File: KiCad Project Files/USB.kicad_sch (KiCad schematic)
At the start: 0 parts

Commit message: Complete schematic aside from switch matrix, and rename project
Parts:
- added C_LD01, C_LD02: 1u, symbol Device:C_Small
- added F1: 500mA, symbol Device:Polyfuse_Small
- added J1: SM04B, symbol Connector:Conn_01x04_Female
- added U4: PRTR5V0U2X, symbol cipulot_parts:PRTR5V0U2X
- added U?: XC6206PxxxMR, Package_TO_SOT_SMD:SOT-23, symbol Regulator_Linear:XC6206PxxxMR
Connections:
- new net +3V3: C_LD02.1, U?.2 (VO)
- new net +5V: C_LD01.1, F1.2, J1.1 (Pin_1), U?.3 (VI)
- new net D+: J1.3 (Pin_3), U4.2 (IO1)
- new net D-: J1.2 (Pin_2), U4.3 (IO2)
- new net GND: C_LD01.2, C_LD02.2, J1.4 (Pin_4), U4.1 (GND), U?.1 (GND)
- new net VCC: F1.1, U4.4 (VCC)
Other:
- note added: "ESD, Power Regulation & Protection"
- note added: "JST"

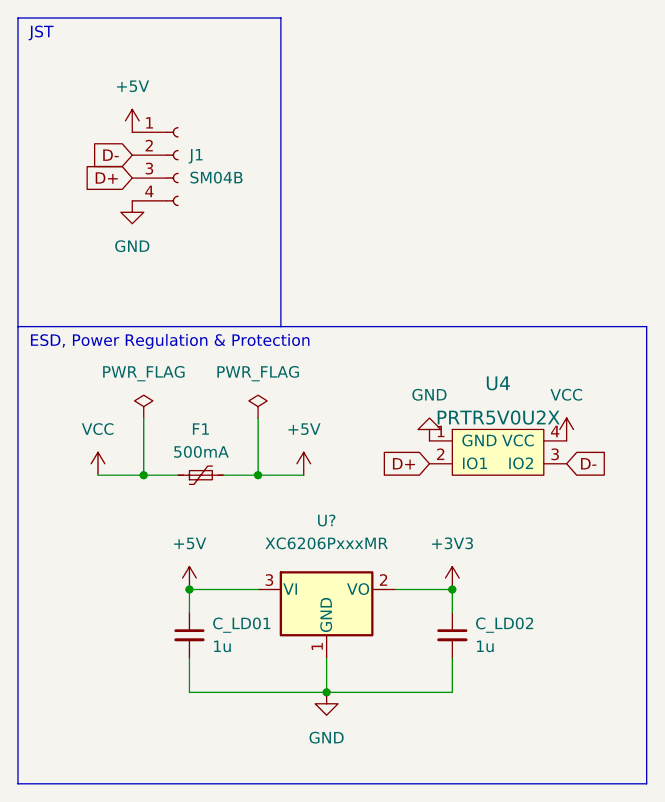
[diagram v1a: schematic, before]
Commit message: Finish schematic, annotate footprints, start pcb creation
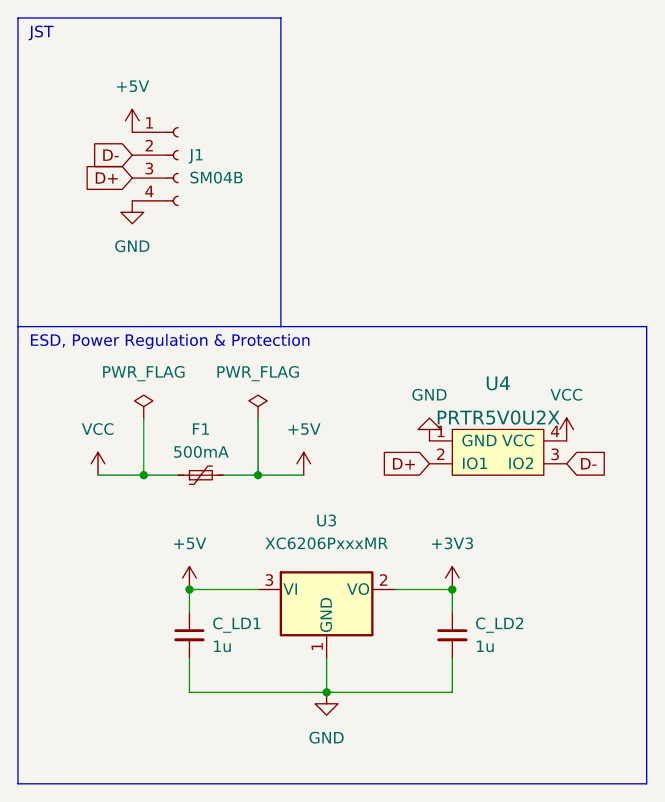
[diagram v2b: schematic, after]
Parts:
- C_LD1: renamed from C_LD01; footprint (none) -> Capacitor_SMD:C_0402_1005Metric
- C_LD2: renamed from C_LD02; footprint (none) -> Capacitor_SMD:C_0402_1005Metric
- F1: footprint (none) -> Fuse:Fuse_0805_2012Metric
- J1: footprint (none) -> Connector_JST:JST_SH_SM04B-SRSS-TB_1x04-1MP_P1.00mm_Horizontal
- U4: footprint (none) -> random-keyboard-parts:SOT143B
- gave numbers to parts that had none: 1
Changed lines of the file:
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@@
   (symbol (lib_id "power:+5V") (at 31.75 76.2 0) (unit 1)
     (in_bom yes) (on_board yes) (fields_autoplaced)
-    (property "Reference" "#PWR?" (id 0) (at 31.75 80.01 0)
+    (property "Reference" "#PWR0123" (id 0) (at 31.75 80.01 0)
       (effects (font (size 1.27 1.27)) hide)
     )
@@
       (effects (font (size 1.27 1.27)) (justify left))
     )
-    (property "Footprint" "" (id 2) (at 30.48 27.94 0)
+    (property "Footprint" "Connector_JST:JST_SH_SM04B-SRSS-TB_1x04-1MP_P1.00mm_Horizontal" (id 2) (at 30.48 27.94 0)
       (effects (font (size 1.27 1.27)) hide)
     )
@@
   (symbol (lib_id "Device:C_Small") (at 31.75 81.28 0) (unit 1)
     (in_bom yes) (on_board yes) (fields_autoplaced)
-    (property "Reference" "C_LD01" (id 0) (at 34.29 80.0162 0)
+    (property "Reference" "C_LD1" (id 0) (at 34.29 80.0162 0)
       (effects (font (size 1.27 1.27)) (justify left))
     )
@@
       (effects (font (size 1.27 1.27)) (justify left))
     )
-    (property "Footprint" "" (id 2) (at 31.75 81.28 0)
+    (property "Footprint" "Capacitor_SMD:C_0402_1005Metric" (id 2) (at 31.75 81.28 0)
       (effects (font (size 1.27 1.27)) hide)
     )
@@
   (symbol (lib_id "power:PWR_FLAG") (at 26.67 57.15 0) (unit 1)
     (in_bom yes) (on_board yes) (fields_autoplaced)
-    (property "Reference" "#FLG?" (id 0) (at 26.67 55.245 0)
+    (property "Reference" "#FLG0101" (id 0) (at 26.67 55.245 0)
       (effects (font (size 1.27 1.27)) hide)
     )
@@
   (symbol (lib_id "power:VCC") (at 73.66 59.69 0) (unit 1)
     (in_bom yes) (on_board yes) (fields_autoplaced)
-    (property "Reference" "#PWR?" (id 0) (at 73.66 63.5 0)
+    (property "Reference" "#PWR0119" (id 0) (at 73.66 63.5 0)
       (effects (font (size 1.27 1.27)) hide)
     )
@@
   (symbol (lib_id "power:GND") (at 58.42 59.69 180) (unit 1)
     (in_bom yes) (on_board yes) (fields_autoplaced)
-    (property "Reference" "#PWR?" (id 0) (at 58.42 53.34 0)
+    (property "Reference" "#PWR0118" (id 0) (at 58.42 53.34 0)
       (effects (font (size 1.27 1.27)) hide)
     )
@@
   (symbol (lib_id "power:+5V") (at 44.45 63.5 0) (unit 1)
     (in_bom yes) (on_board yes) (fields_autoplaced)
-    (property "Reference" "#PWR?" (id 0) (at 44.45 67.31 0)
+    (property "Reference" "#PWR0124" (id 0) (at 44.45 67.31 0)
       (effects (font (size 1.27 1.27)) hide)
     )
@@
   (symbol (lib_id "Device:C_Small") (at 60.96 81.28 0) (unit 1)
     (in_bom yes) (on_board yes) (fields_autoplaced)
-    (property "Reference" "C_LD02" (id 0) (at 63.5 80.0162 0)
+    (property "Reference" "C_LD2" (id 0) (at 63.5 80.0162 0)
       (effects (font (size 1.27 1.27)) (justify left))
     )
@@
       (effects (font (size 1.27 1.27)) (justify left))
     )
-    (property "Footprint" "" (id 2) (at 60.96 81.28 0)
+    (property "Footprint" "Capacitor_SMD:C_0402_1005Metric" (id 2) (at 60.96 81.28 0)
       (effects (font (size 1.27 1.27)) hide)
     )
@@
   (symbol (lib_id "power:GND") (at 25.4 33.02 0) (unit 1)
     (in_bom yes) (on_board yes) (fields_autoplaced)
-    (property "Reference" "#PWR?" (id 0) (at 25.4 39.37 0)
+    (property "Reference" "#PWR0125" (id 0) (at 25.4 39.37 0)
       (effects (font (size 1.27 1.27)) hide)
     )
@@
   (symbol (lib_id "power:GND") (at 46.99 87.63 0) (unit 1)
     (in_bom yes) (on_board yes) (fields_autoplaced)
-    (property "Reference" "#PWR?" (id 0) (at 46.99 93.98 0)
+    (property "Reference" "#PWR0120" (id 0) (at 46.99 93.98 0)
       (effects (font (size 1.27 1.27)) hide)
     )
@@
   (symbol (lib_id "power:+3V3") (at 60.96 76.2 0) (unit 1)
     (in_bom yes) (on_board yes) (fields_autoplaced)
-    (property "Reference" "#PWR?" (id 0) (at 60.96 80.01 0)
+    (property "Reference" "#PWR0121" (id 0) (at 60.96 80.01 0)
       (effects (font (size 1.27 1.27)) hide)
     )
@@
       (effects (font (size 1.524 1.524)))
     )
-    (property "Footprint" "" (id 2) (at 66.04 60.96 0)
+    (property "Footprint" "random-keyboard-parts:SOT143B" (id 2) (at 66.04 60.96 0)
       (effects (font (size 1.524 1.524)) hide)
     )
@@
   (symbol (lib_id "Regulator_Linear:XC6206PxxxMR") (at 46.99 76.2 0) (unit 1)
     (in_bom yes) (on_board yes) (fields_autoplaced)
-    (property "Reference" "U?" (id 0) (at 46.99 68.58 0))
+    (property "Reference" "U3" (id 0) (at 46.99 68.58 0))
     (property "Value" "XC6206PxxxMR" (id 1) (at 46.99 71.12 0))
     (property "Footprint" "Package_TO_SOT_SMD:SOT-23" (id 2) (at 46.99 70.485 0)
@@
   (symbol (lib_id "power:+5V") (at 25.4 25.4 0) (unit 1)
     (in_bom yes) (on_board yes) (fields_autoplaced)
-    (property "Reference" "#PWR?" (id 0) (at 25.4 29.21 0)
+    (property "Reference" "#PWR0126" (id 0) (at 25.4 29.21 0)
       (effects (font (size 1.27 1.27)) hide)
     )
@@
     (property "Reference" "F1" (id 0) (at 33.02 58.42 90))
     (property "Value" "500mA" (id 1) (at 33.02 60.96 90))
-    (property "Footprint" "" (id 2) (at 38.1 62.23 0)
+    (property "Footprint" "Fuse:Fuse_0805_2012Metric" (id 2) (at 38.1 62.23 0)
       (effects (font (size 1.27 1.27)) (justify left) hide)
     )
@@
   (symbol (lib_id "power:PWR_FLAG") (at 39.37 57.15 0) (unit 1)
     (in_bom yes) (on_board yes) (fields_autoplaced)
-    (property "Reference" "#FLG?" (id 0) (at 39.37 55.245 0)
+    (property "Reference" "#FLG0102" (id 0) (at 39.37 55.245 0)
       (effects (font (size 1.27 1.27)) hide)
     )
@@
   (symbol (lib_id "power:VCC") (at 21.59 63.5 0) (unit 1)
     (in_bom yes) (on_board yes) (fields_autoplaced)
-    (property "Reference" "#PWR?" (id 0) (at 21.59 67.31 0)
-      (effects (font (size 1.27 1.27)) hide)
-    )
+    (property "Reference" "#PWR0122" (id 0) (at 21.59 67.31 0)
+      (effects (font (size 1.27 1.27)) hide)
+    )

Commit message: Finish PCB and create production files
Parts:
- removed F1: 500mA, Fuse:Fuse_0805_2012Metric, symbol Device:Polyfuse_Small
- removed U4: PRTR5V0U2X, random-keyboard-parts:SOT143B, symbol cipulot_parts:PRTR5V0U2X
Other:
- moved on the sheet: C_LD1, C_LD2, U3
